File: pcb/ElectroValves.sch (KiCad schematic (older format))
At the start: 33 parts, among them J3 Conn_Load, J4 Conn_Load, J5 Conn_Load, J6 Conn_Load, U11 AQH3213AX, U12 AQH3213AX, U13 AQH3213AX, U14 AQH3213AX, U15 PCAL6416A, U3 TLP240D, U4 TLP240D, U5 TLP240D, U6 TLP240D, U7 TLP240D, U8 TLP240D

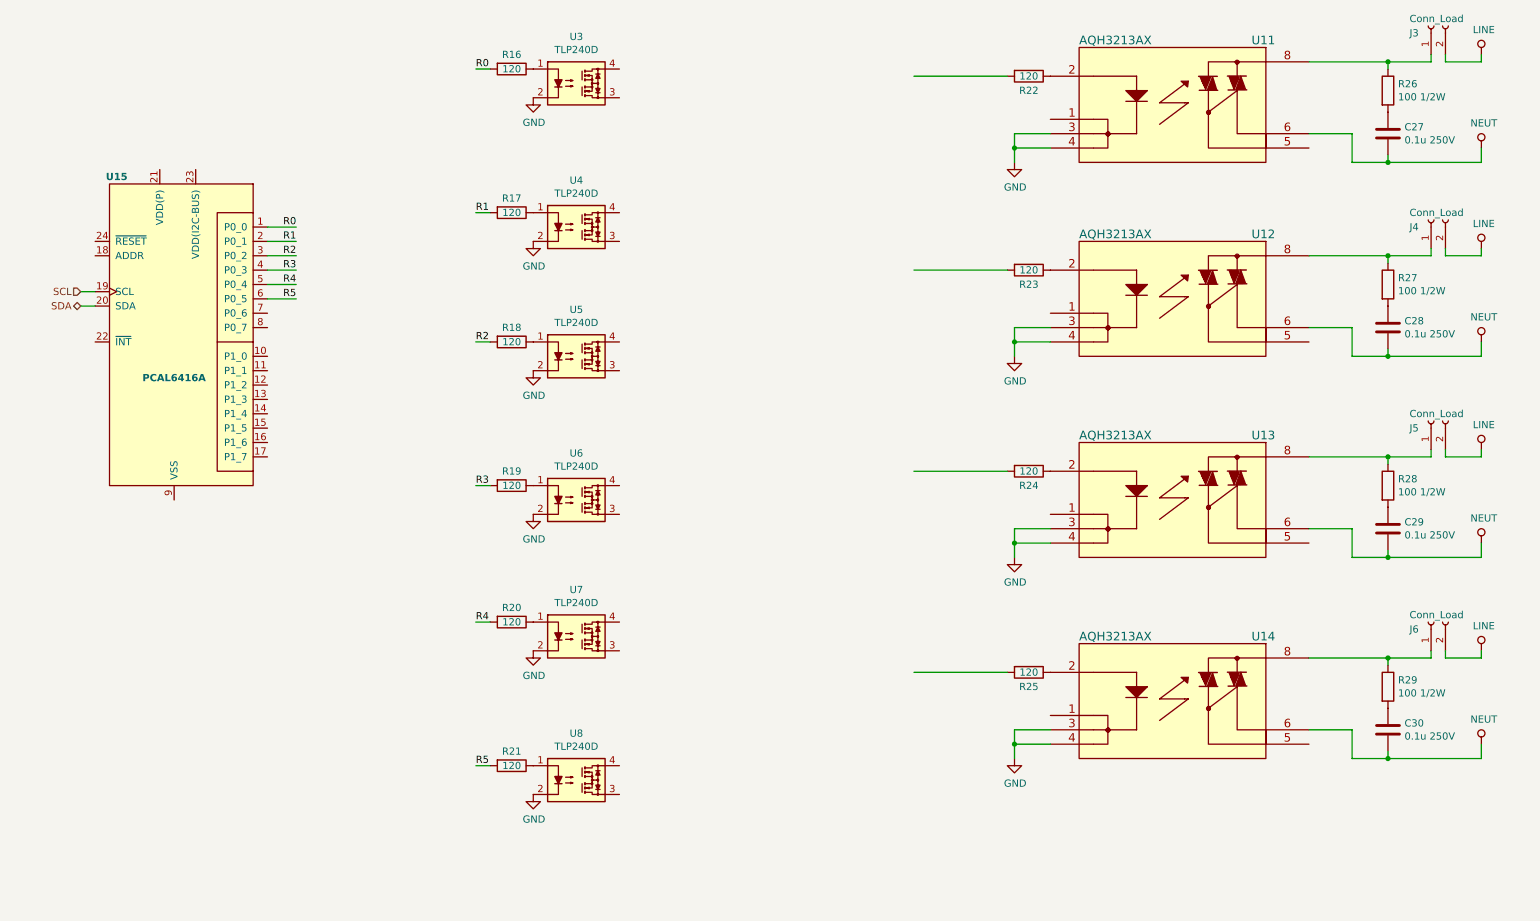
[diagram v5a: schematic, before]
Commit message: added connections to ElectroValves sheet
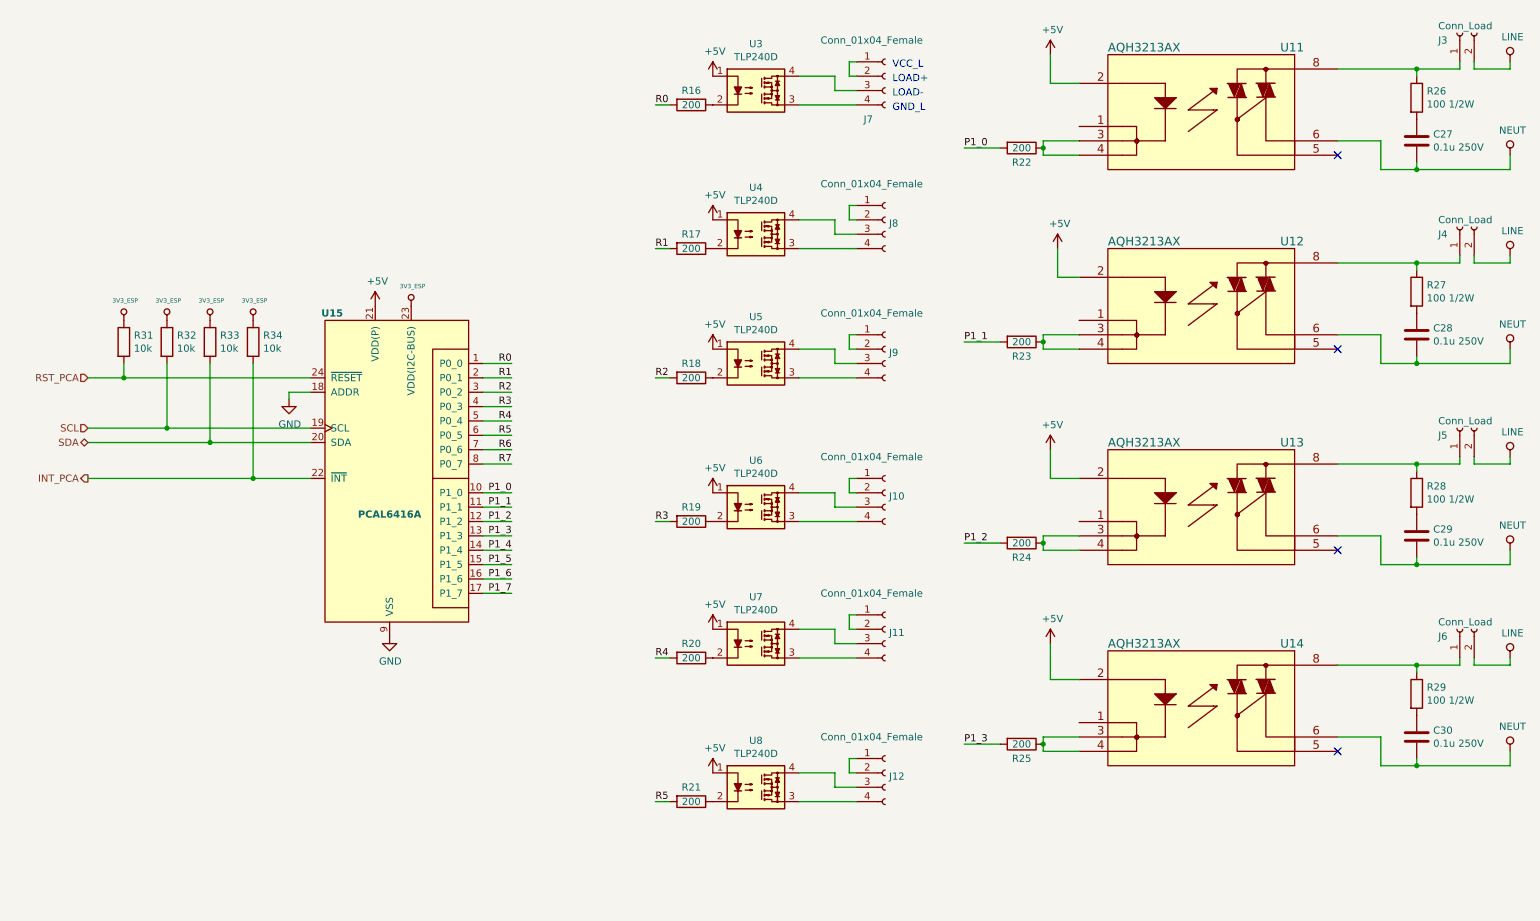
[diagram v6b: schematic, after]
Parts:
- added J10, J11, J12, J7, J8, J9: Conn_01x04_Female, symbol BarrelConnector:Conn_01x04_Female
- added R31, R32, R33, R34: 10k, Resistors_SMD:R_0603, symbol Device:R
- R16, R17, R18, R19, R20, R21: value 120 -> 200
- R22, R23, R24, R25: value 120 -> 200; footprint (none) -> Resistors_SMD:R_0603
- U15: DigiKey (none) -> 568-9946-1-ND
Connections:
- net labels added: +5V, 3V3_ESP, INT_PCA, P1_0, P1_1, P1_2, P1_3, P1_4, P1_5, P1_6, P1_7, R6, R7, RST_PCA
- wire segments 86 -> 158
- no-connect marks 0 -> 4
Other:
- note added: "GND_L"
- note added: "LOAD+"
- note added: "LOAD-"
- note added: "VCC_L"
- moved on the sheet: C27, C28, C29, C30, J3, J4, J5, J6, R16, R17, R18, R19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

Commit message: led drive transistors
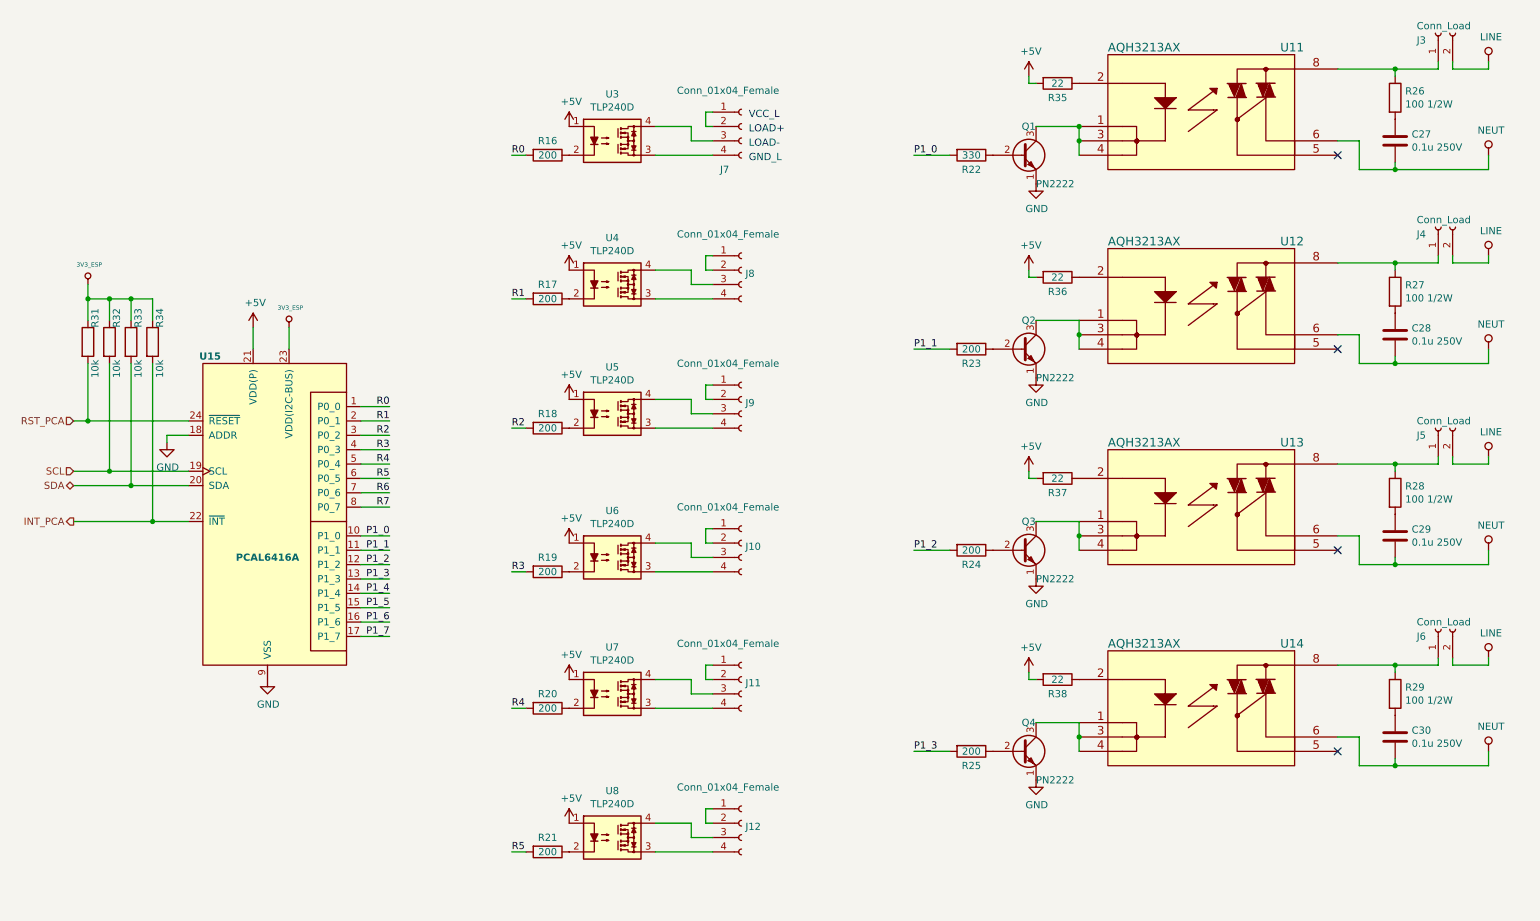
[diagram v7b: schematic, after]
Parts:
- added Q1, Q2, Q3, Q4: PN2222, SMD:SOT23_Transistor, symbol Transistor_BJT:PN2222A
- added R35, R36, R37, R38: 22, Resistor_SMD:R_0402_1005Metric, symbol Device:R
- R22: value 200 -> 330; footprint Resistors_SMD:R_0603 -> Resistor_SMD:R_0402_1005Metric
- R23, R24, R25, R31, R32, R33, R34: footprint Resistors_SMD:R_0603 -> Resistor_SMD:R_0402_1005Metric
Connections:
- net +5V: now also R35.2, R36.2, R37.2, R38.2; no longer U11.2, U12.2, U13.2, U14.2
- net GND: now also Q1.1 (E), Q2.1 (E), Q3.1 (E), Q4.1 (E)
- net at U11.1: now also U11.3, U11.4, Q1.3 (C)
- net at U12.1: now also U12.3, U12.4, Q2.3 (C)
- net at U13.1: now also U13.3, U13.4, Q3.3 (C)
- net at U14.1: now also U14.3, U14.4, Q4.3 (C)
- new net: R35.1, U11.2
- new net: Q1.2 (B), R22.1
- new net: R36.1, U12.2
- new net: Q2.2 (B), R23.1
- new net: R37.1, U13.2
- new net: Q3.2 (B), R24.1
- new net: R38.1, U14.2
- new net: Q4.2 (B), R25.1
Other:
- moved on the sheet: C27, C28, C29, C30, J10, J11, J12, J3, J4, J5, J6, J7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
